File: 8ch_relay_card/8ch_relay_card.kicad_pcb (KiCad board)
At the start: 2 copper layers, 78 x 150 mm, 97 parts, among them J1 CamdenBoss CTB3051/10BK, J10 jmp_3way, J11 TruConnect XY-305, J12 TruConnect XY-305, J13 TruConnect XY-305, J14 TruConnect XY-305, J15 TruConnect XY-305, J16 TruConnect XY-305, J17 TruConnect XY-305, J18 TruConnect XY-305, J19 jmp_2way, J2 jmp_3way, J20 TruConnect 21-3000, J3 jmp_3way, J4 jmp_3way, J5 jmp_3way, J6 jmp_3way, J7 jmp_3way, J8 jmp_3way, J9 jmp_3way, Q1 2N7002, Q10 2N7002, Q11 2N7002, Q12 2N7002, Q13 2N7002, Q14 2N7002, Q15 2N7002, Q16 2N7002, Q17 STD12NF06L, Q2 2N7002, Q3 2N7002, Q4 2N7002, Q5 2N7002, Q6 2N7002, Q7 2N7002, Q8 2N7002, Q9 2N7002, U1 ULN2803

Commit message: Removed bi-colour LEDs and reverted to single colour LEDs.  PCB Design finished.
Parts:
- removed J19: jmp_2way, bjh-kicad-connector-fp:HEAD-1row-2.54mm-2way
- removed Q1, Q10, Q11, Q12, Q13, Q14, Q15, Q16, Q2, Q3, Q4, Q5, Q6, Q7, Q8, Q9: 2N7002, TO_SOT_Packages_SMD:SOT-23
- removed R17, R18, R19, R20, R25, R26, R27, R28, R29, R30, R31, R32: 470, Resistors_SMD:R_0805
- removed R21, R22, R23, R24: 10k, Resistors_SMD:R_0805
- removed the REF** at (117.0, 28.0)
- removed the REF** at (48.0, 28.0)
- removed the REF** at (117.0, 170.0)
- removed the REF** at (48.0, 170.0)
- added G***: LOGO, bjh-kicad-logo-fp:logo_10mm_hoskins_tech, F.Cu at (74.0, 168.5)
- added REF**: MountingHole_3-0mm, bjh-kicad-mountingholes-fp:MountingHole_3-0mm, F.Cu at (46.5, 27.0)
- added REF**: MountingHole_3-0mm, bjh-kicad-mountingholes-fp:MountingHole_3-0mm, F.Cu at (118.5, 27.0)
- added REF**: MountingHole_3-0mm, bjh-kicad-mountingholes-fp:MountingHole_3-0mm, F.Cu at (46.5, 171.0)
- added REF**: MountingHole_3-0mm, bjh-kicad-mountingholes-fp:MountingHole_3-0mm, F.Cu at (118.5, 171.0)
- D1, D2, D3, D4, D5, D6, D7, D8: value L-59EGW -> LED; footprint LEDs:LED-5MM-3 -> LEDs:LED-5MM
- R10, R9: value 10k -> 470; moved to F.Cu
- R11, R12: value 10k -> 470
- R13: moved to F.Cu
- moved R16 229.3 mm to (106.5, 150.5), turned to 90 degrees
- moved R14 224.2 mm to (106.5, 117.5), turned to 90 degrees
- moved R11 206.0 mm to (106.5, 68.0), turned to 90 degrees
- moved R12 204.8 mm to (106.5, 84.5), turned to 90 degrees
- moved R15 191.9 mm to (106.5, 134.0), turned to 90 degrees
- moved R13 68.3 mm to (106.5, 101.0), turned to 90 degrees
- moved R9 28.1 mm to (106.5, 35.0), turned to 90 degrees
- moved R10 28.1 mm to (106.5, 51.5), turned to 90 degrees
- moved G*** 20.6 mm to (77.0, 29.5)
- moved D1 1.00 mm to (106.5, 42.5)
- moved D2 1.00 mm to (106.5, 59.0)
- moved D3 1.00 mm to (106.5, 75.5)
- moved D4 1.00 mm to (106.5, 92.0)
- moved D5 1.00 mm to (106.5, 108.5)
- moved D7 1.00 mm to (106.5, 141.5)
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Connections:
- D1 pad 1: Net-(D1-Pad1) -> OUT1
- D1 pad 2: GND -> Net-(D1-Pad2)
- D2 pad 1: Net-(D2-Pad1) -> OUT2
- D2 pad 2: GND -> Net-(D2-Pad2)
- D3 pad 1: Net-(D3-Pad1) -> OUT3
- D3 pad 2: GND -> Net-(D3-Pad2)
- D4 pad 1: Net-(D4-Pad1) -> OUT4
- D4 pad 2: GND -> Net-(D4-Pad2)
- D5 pad 1: Net-(D5-Pad1) -> OUT5
- D5 pad 2: GND -> Net-(D5-Pad2)
- D6 pad 1: Net-(D6-Pad1) -> OUT6
- D6 pad 2: GND -> Net-(D6-Pad2)
- D7 pad 1: Net-(D7-Pad1) -> OUT7
- D7 pad 2: GND -> Net-(D7-Pad2)
- D8 pad 1: Net-(D8-Pad1) -> OUT8
- D8 pad 2: GND -> Net-(D8-Pad2)
- R10 pad 1: +12V_SW -> Net-(D2-Pad2)
- R10 pad 2: OUT2 -> +12V
- R11 pad 1: +12V_SW -> Net-(D3-Pad2)
- R11 pad 2: OUT3 -> +12V
- R12 pad 1: +12V_SW -> Net-(D4-Pad2)
- R12 pad 2: OUT4 -> +12V
- R13 pad 1: +12V_SW -> Net-(D5-Pad2)
- R13 pad 2: Net-(D1-Pad3) -> +12V
- R14 pad 1: +12V_SW -> Net-(D6-Pad2)
- R14 pad 2: Net-(D2-Pad3) -> +12V
- R15 pad 1: +12V_SW -> Net-(D7-Pad2)
- R15 pad 2: Net-(D3-Pad3) -> +12V
- R16 pad 1: +12V_SW -> Net-(D8-Pad2)
- R16 pad 2: Net-(D4-Pad3) -> +12V
- R9 pad 1: +12V_SW -> Net-(D1-Pad2)
- R9 pad 2: OUT1 -> +12V
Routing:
- net +12V: track 52.8 -> 436.0 mm
- net Net-(D1-Pad1): track 43.4 -> 0.00 mm, vias 1 -> 0
- net Net-(D1-Pad3): track 40.9 -> 0.00 mm, vias 1 -> 0
- net OUT8: track 54.2 -> 94.4 mm
- net OUT6: track 24.9 -> 65.0 mm
- net OUT4: track 15.6 -> 55.7 mm
- net OUT5: track 11.4 -> 51.2 mm
- net OUT2: track 43.0 -> 82.8 mm
- net OUT3: track 29.3 -> 69.1 mm
- net OUT7: track 38.8 -> 78.3 mm
- net OUT1: track 62.4 -> 96.0 mm
- net GND: track 191.9 -> 161.5 mm, vias 1 -> 0
- net RL3_NC: track 7.50 -> 37.1 mm
- net +12V_SW: track 16.5 -> 0.00 mm
- net Net-(D8-Pad2): track 0.00 -> 4.01 mm
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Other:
- net class Default: clearance 0.4 -> 0.2
- rule trace_clearance: 0.4 -> 0.2
- board text added: "2D DATA MATRIX AREA"
- board text added: "8CH_RELAY_CARD V1.0 B.HOSKINS 2017-11-05"

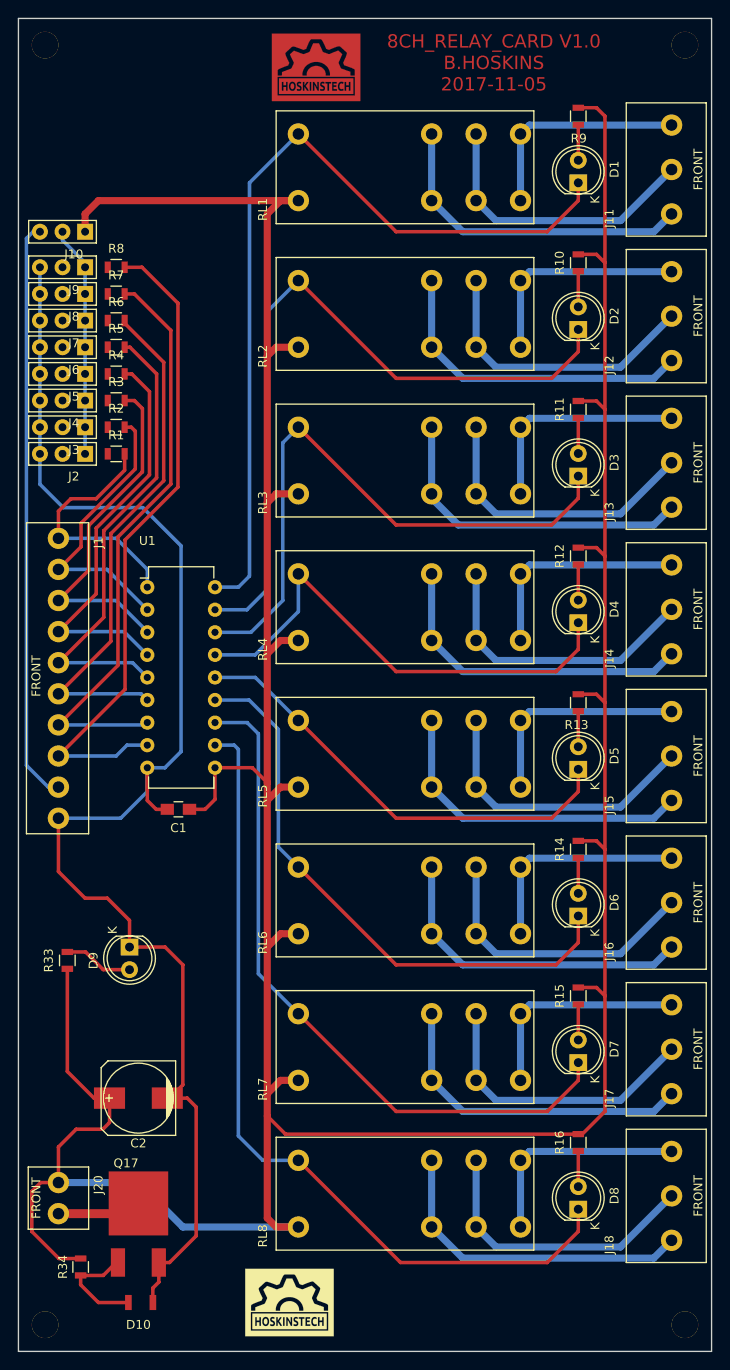
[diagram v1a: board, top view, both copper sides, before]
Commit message: V1.1: Changed relay layout to improve solderability, especially on home-made PCBs without through-plating. Changed output connector to a all-in-one stacked version
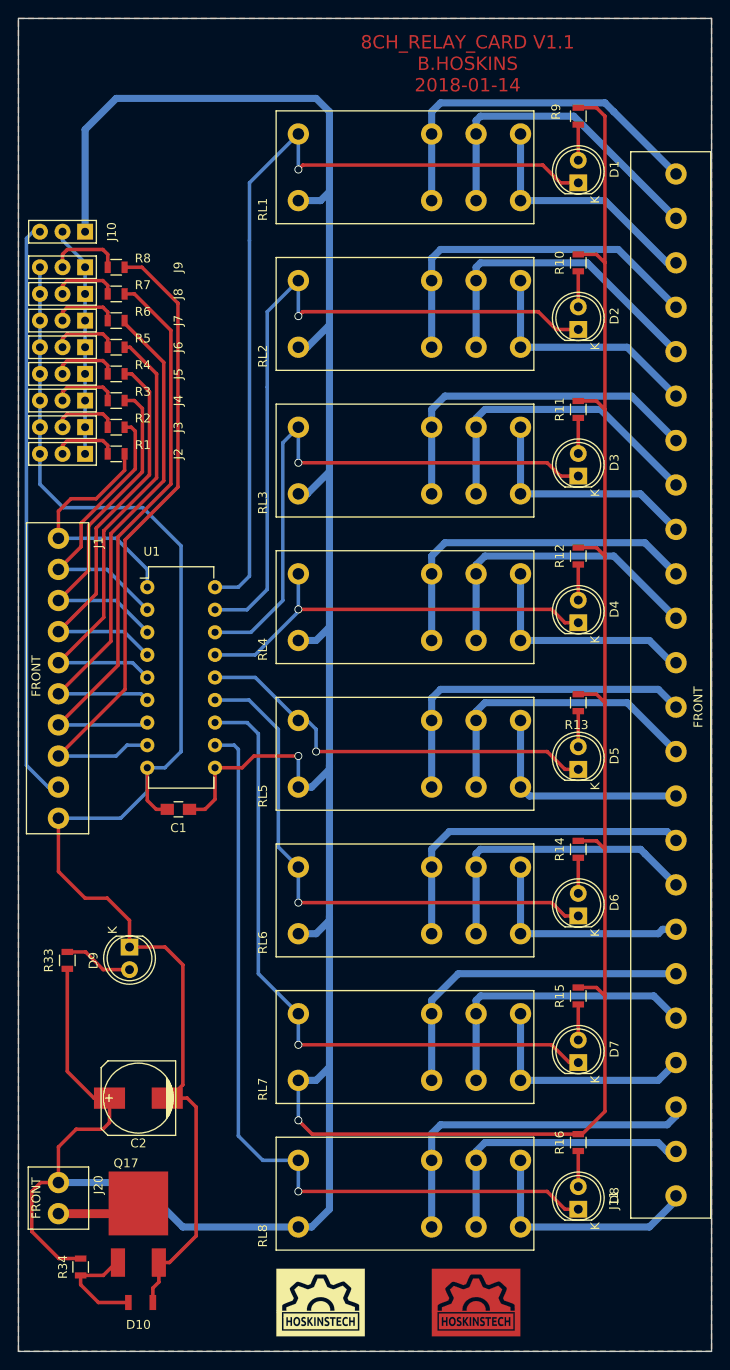
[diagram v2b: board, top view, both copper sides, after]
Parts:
- removed J12, J13, J14, J15, J16, J17, J18: TruConnect XY-305, bjh-kicad-connector-fp:TruConnect_21-1812
- removed REF** (x4): MountingHole_3-0mm, bjh-kicad-mountingholes-fp:MountingHole_3-0mm
- J11: value TruConnect XY-305 -> RELAY OUTPUTS; footprint bjh-kicad-connector-fp:TruConnect_21-1812 -> bjh-kicad-connector-fp:TruConnect_21-1812_x8_stacked
- moved G*** 140.2 mm to (95.0, 168.5)
- moved J11 110.5 mm to (117.5, 156.5)
- moved G*** 3.50 mm to (77.5, 168.5)
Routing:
- net +12V: track 436.0 -> 471.3 mm, vias 0 -> 2
- net Net-(J9-Pad2): track 0.00 -> 8.45 mm
- net OUT4: track 55.7 -> 47.8 mm, vias 0 -> 1
- net Net-(J8-Pad2): track 0.00 -> 7.45 mm
- net Net-(J7-Pad2): track 0.00 -> 7.45 mm
- net Net-(J6-Pad2): track 0.00 -> 7.45 mm
- net Net-(J5-Pad2): track 0.00 -> 7.45 mm
- net Net-(J4-Pad2): track 0.00 -> 7.45 mm
- net Net-(J3-Pad2): track 0.00 -> 7.45 mm
- net Net-(J2-Pad2): track 0.00 -> 7.45 mm
- net OUT5: track 51.2 -> 46.6 mm, vias 0 -> 1
- net RL1_NC: track 36.8 -> 41.2 mm
- net OUT8: track 94.4 -> 90.0 mm, vias 0 -> 1
- net OUT6: track 65.0 -> 61.1 mm, vias 0 -> 1
- net RL2_NC: track 36.8 -> 40.6 mm
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- added copper zone on B.Cu, net GND
- added copper zone on F.Cu, net GND
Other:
- net class Default: via_dia 0.6 -> 0.7
- net class PowerTracks: via_dia 0.6 -> 0.8
- board text added: "8CH_RELAY_CARD V1.1 B.HOSKINS 2018-01-14"
- board text removed: "8CH_RELAY_CARD V1.0 B.HOSKINS 2017-11-05"
